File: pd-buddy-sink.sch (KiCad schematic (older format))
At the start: 2 parts

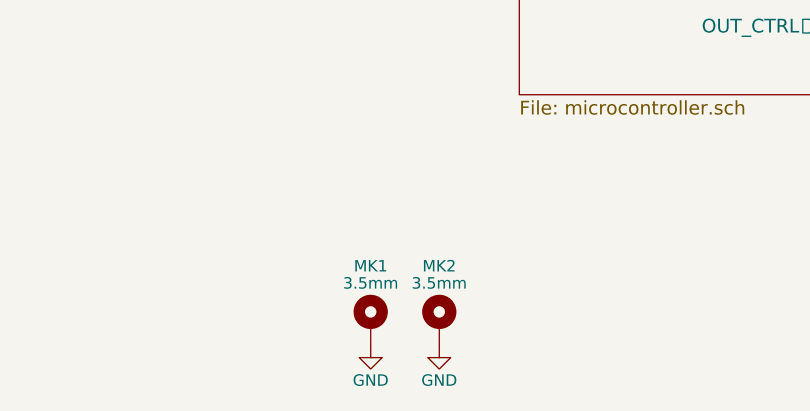
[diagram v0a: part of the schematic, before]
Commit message: 4-layer board with smaller components
This is a major change!  Almost all the components have changed to
smaller versions, with 0603 and 0402 passives and a QFN microcontroller.
The board now has four layers, with internal layers used for VBUS and
GND.  The board now measures a mere 25×30 mm!  The SWD header and Boot
switch footprints have been moved to the bottom to help with this
shrinkage.  Two test points were added to the bottom as well to make it
possible to power the board without using the USB connector.  The
mounting holes are now slightly smaller (better sized for M3), and only
17 mm apart instead of the old 18 mm.

To sum up, everything is smaller and that's almost entirely a good
thing, except now it's not really possible to build one by hand.
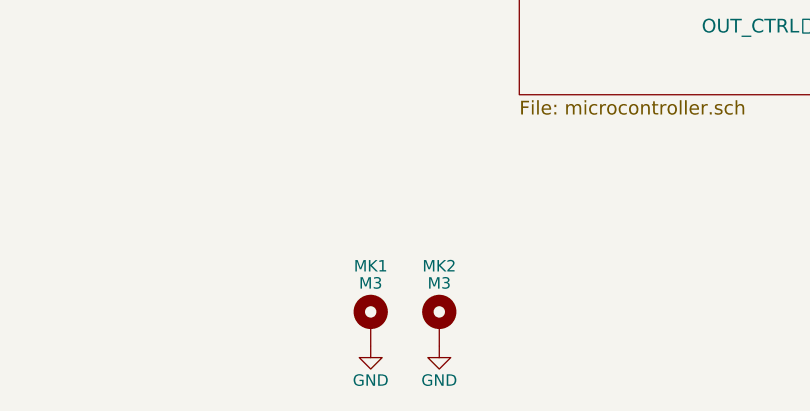
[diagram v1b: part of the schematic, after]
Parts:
- MK1, MK2: value 3.5mm -> M3; footprint Mounting_Holes:MountingHole_3.5mm_Pad_Via -> Mounting_Holes:MountingHole_3.2mm_M3_Pad_Via
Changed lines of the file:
@@
 P 4050 5700
 F 0 "MK1" H 4050 5950 50  0000 C CNN
-F 1 "3.5mm" H 4050 5875 50  0000 C CNN
-F 2 "Mounting_Holes:MountingHole_3.5mm_Pad_Via" H 4050 5700 60  0001 C CNN
+F 1 "M3" H 4050 5875 50  0000 C CNN
+F 2 "Mounting_Holes:MountingHole_3.2mm_M3_Pad_Via" H 4050 5700 60  0001 C CNN
 F 3 "" H 4050 5700 60  0001 C CNN
 	1    4050 5700
@@
 P 4350 5700
 F 0 "MK2" H 4350 5950 50  0000 C CNN
-F 1 "3.5mm" H 4350 5875 50  0000 C CNN
-F 2 "Mounting_Holes:MountingHole_3.5mm_Pad_Via" H 4350 5700 60  0001 C CNN
+F 1 "M3" H 4350 5875 50  0000 C CNN
+F 2 "Mounting_Holes:MountingHole_3.2mm_M3_Pad_Via" H 4350 5700 60  0001 C CNN
 F 3 "" H 4350 5700 60  0001 C CNN
 	1    4350 5700
